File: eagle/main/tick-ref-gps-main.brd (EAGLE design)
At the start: 91.4 x 106.3 mm, 53 parts, among them CN1 1PPS Out, CN2 ISP, CN3 RS232, CN4 Power In, CN5 Serial Program, U1 ATMEGA168-AU, U2 AS1115, U3 MAX232, U4 LM2931_FIXED, X1 16MHz

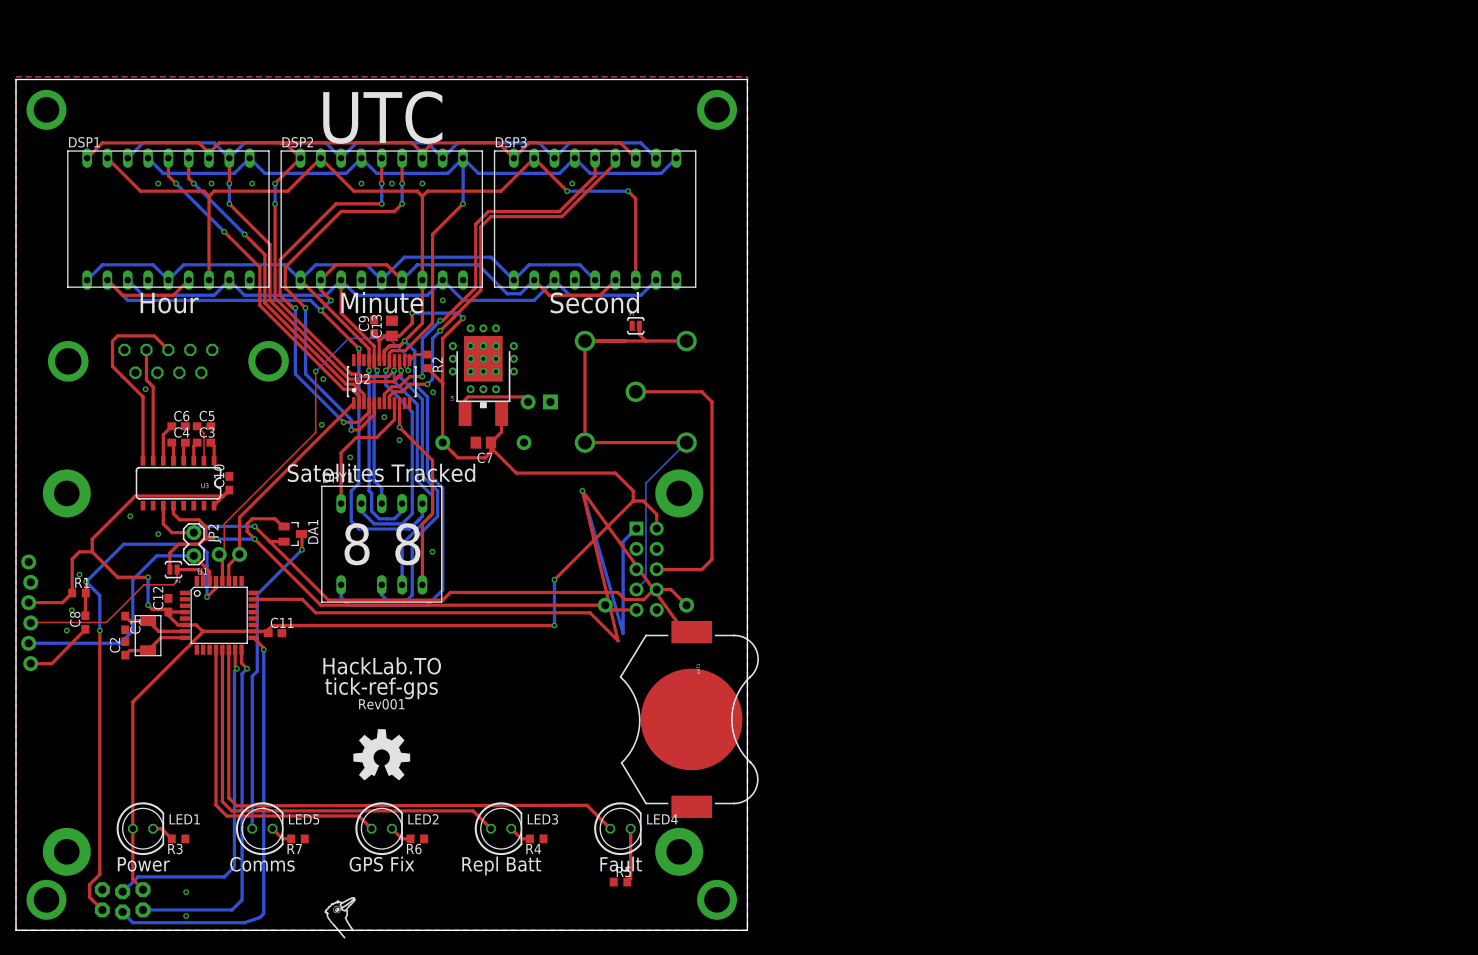
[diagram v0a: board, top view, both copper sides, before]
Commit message: New main board design schematic done, half-routed.
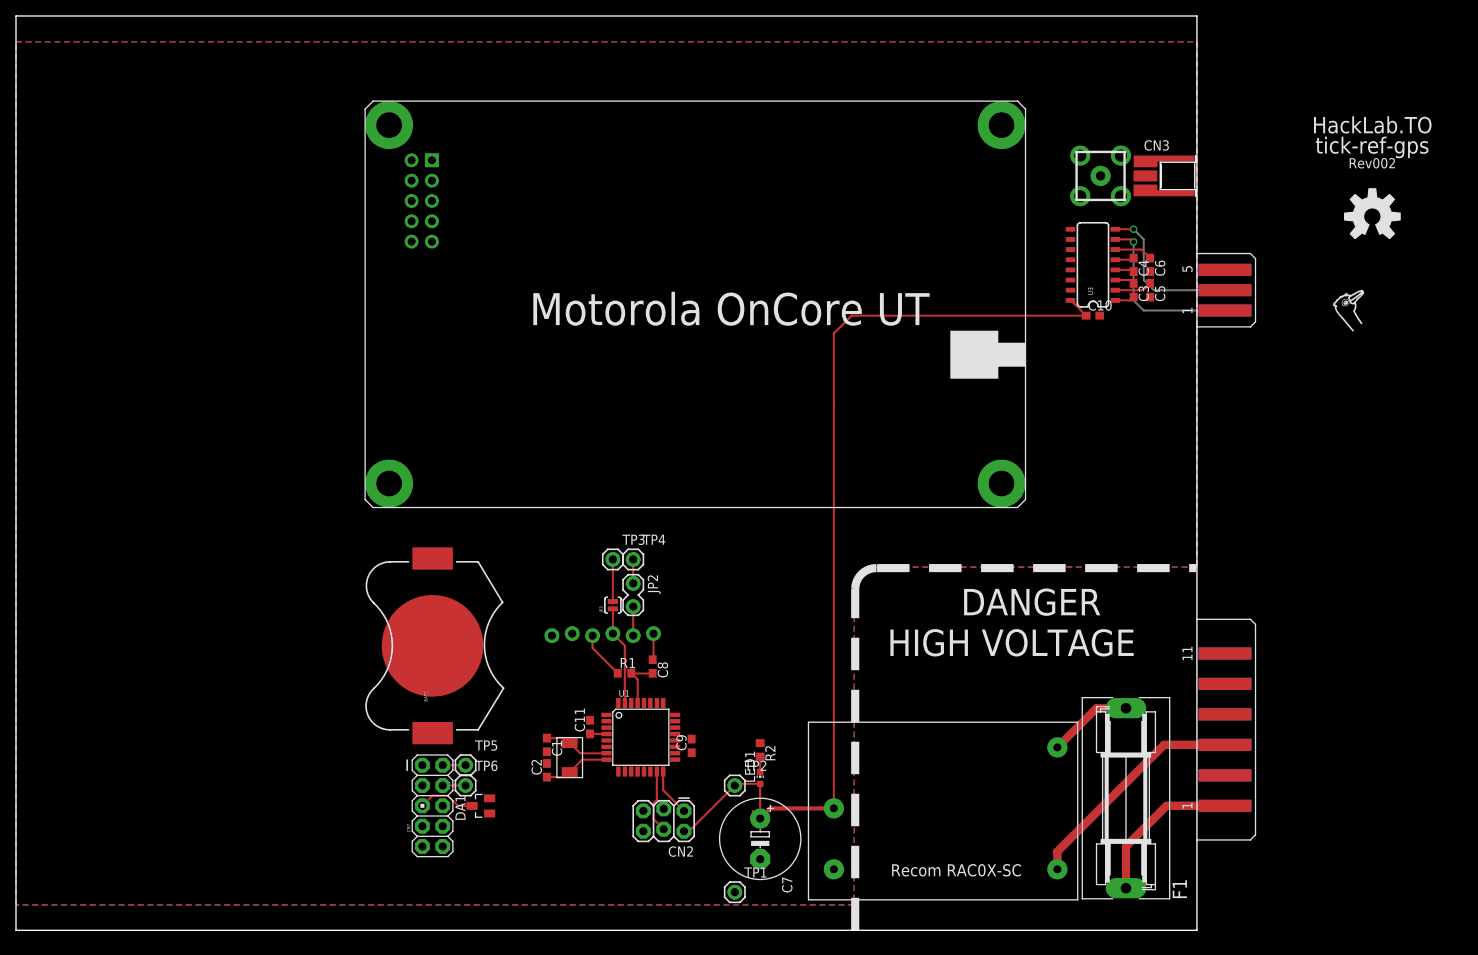
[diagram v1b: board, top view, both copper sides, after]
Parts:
- removed C12: 0.1uF, rcl:C0603
- removed C13: 2.2uF, rcl:C0805
- removed DPY1: Sats Tracked, led-sen:LDD-F302NI
- removed DSP1: Hour, display-hp:HDSP-R
- removed DSP2: Minute, display-hp:HDSP-R
- removed DSP3: Second, display-hp:HDSP-R
- removed JP1: PPS RTN Link, SparkFun:SJ_2S-NO
- removed LED2: GPS Fix, led:LED5MM
- removed LED3: Replace Batt, led:LED5MM
- removed LED4: Fault, led:LED5MM
- removed LED5: Comms, led:LED5MM
- removed R3, R4, R5: 1.8k, rcl:R0603
- removed R6: 100, rcl:R0603
- removed R7: 18, rcl:R0603
- removed U4: LM2931_FIXED, SparkFun-PowerIC:DPAK
- added CN6: Backplane, con-sen:EDGECON-M-0.1-6
- added CN7: Front Panel, SparkFun-Connectors:AVR_ICSP
- added F1: 1A Slow Blow, fuse:SH22,5A
- C7: value 2.2uF -> 330uF; device rcl:C0805 -> rcl:E5-10,5
- CN1: value 1PPS Out -> Power In; device con-coax:B35N57 -> con-sen:EDGECON-M-0.15-12
- CN3: value RS232 -> Ant. BP; device con-subd:F09VP -> con-samtec:MMCX-J-P-X-ST-EM1-MKT
- CN4: value Power In -> Ant. GPS; device SparkFun:MOLEX-1X2_LOCK -> con-sen:MOLEX-MCX-V
- JP3: value Standalone/PC -> PC Listen
- LED1: device led:LED5MM -> led:CHIP-LED0603
- R2: value 15k -> 1.8k
- U2: value AS1115 -> RAC02-05SC; device austria-sen:QSOP24 -> recom-sen:RAC0X-SC
- moved U$2 147.1 mm to (166.4, 76.9)
- moved U$1 141.1 mm to (169.5, 89.2)
- moved CN3 130.3 mm to (147.3, 94.3), flipped to the top, turned to 270 degrees
- moved GPS1 125.6 mm to (123.2, 100.6), flipped to the top
- moved C6 123.1 mm to (141.7, 83.2), turned to 270 degrees
- moved C4 121.4 mm to (139.7, 83.2), turned to 270 degrees
- moved C5 119.5 mm to (141.7, 80.0), turned to 270 degrees
- moved C3 117.8 mm to (139.7, 80.0), turned to 270 degrees
- moved U3 117.5 mm to (134.6, 83.2), turned to 90 degrees
- moved C10 110.0 mm to (134.6, 76.8), turned to 0 degrees
- moved U2 88.2 mm to (114.9, 14.0), turned to 180 degrees
- moved CN1 84.9 mm to (151.1, 25.1), flipped to the top, turned to 90 degrees
- moved LED1 77.4 mm to (93.0, 19.1)
- moved CN4 74.5 mm to (135.6, 94.3), flipped to the top
- moved C8 71.1 mm to (79.6, 33.0), turned to 270 degrees
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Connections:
- removed net CATH_HOUR_LS: DSP1.13, U2.3
- removed net CATH_HOUR_MS: DSP1.14, U2.2
- removed net CATH_MIN_LS: DSP2.13, U2.5
- removed net CATH_MIN_MS: DSP2.14, U2.4
- removed net CATH_SATS_LS: DPY1.5, U2.10
- removed net CATH_SATS_MS: DPY1.10, U2.9
- removed net CATH_SEC_LS: DSP3.13, U2.8
- removed net CATH_SEC_MS: DSP3.14, U2.7
- removed net LED1_R: LED1.K, R3.2
- removed net LED2_R: LED2.K, R6.2
- removed net LED3_R: LED3.K, R4.2
- removed net LED4_R: LED4.K, R5.2
- removed net LED5_D: DA1.3, LED5.A
- removed net LED5_R: LED5.K, R7.2
- removed net LED_ISET: R2.1, U2.13
- removed net LED_SEG_A: DPY1.3, DSP1.11, DSP1.16, DSP2.11, DSP2.16, DSP3.11, DSP3.16, U2.15
- removed net LED_SEG_B: DPY1.9, DSP1.10, DSP1.15, DSP2.10, DSP2.15, DSP3.10, DSP3.15, U2.17
- removed net LED_SEG_C: DPY1.8, DSP1.3, DSP1.8, DSP2.3, DSP2.8, DSP3.3, DSP3.8, U2.20
- removed net LED_SEG_D: DPY1.6, DSP1.2, DSP1.6, DSP2.2, DSP2.6, DSP3.2, DSP3.6, U2.23
- removed net LED_SEG_E: DPY1.7, DSP1.1, DSP1.5, DSP2.1, DSP2.5, DSP3.1, DSP3.5, U2.21
- removed net LED_SEG_F: DPY1.4, DSP1.12, DSP1.18, DSP2.12, DSP2.18, DSP3.12, DSP3.18, U2.16
- removed net LED_SEG_G: DPY1.1, DSP1.17, DSP1.7, DSP2.17, DSP2.7, DSP3.17, DSP3.7, U2.18
- removed net VIN: CN4.2, U4.1
- new net ANTENNA-GND: CN3.2@1, CN4.GND1, CN4.GND2, CN4.GND3, CN4.GND4
- new net ANTENNA-RF: CN3.1, CN4.CTR
- new net LED_COMM: CN7.5, DA1.3
- new net LINE: F1.2, U2.2
- new net LINE-PREFUSE: CN1.1, CN1.2, F1.1
- new net N$1: LED1.C, R2.2
- new net NEUTRAL: CN1.5, CN1.6, U2.1
- new net PE: CN1.11, CN1.12
- net +5V: now also C7.+, CN7.9, U2.4; no longer C12.1, C13.1, C7.1, R2.2, U2.19, U4.3
- net 1PPS: now also CN6.2; no longer CN1.1
- net 1PPS_RTN: now also CN6.6; no longer CN1.2, CN1.3, CN1.4, CN1.5, JP1.2
- net GND: now also C7.-, CN3.2@2, CN3.2@3, CN3.2@4, CN6.5, CN7.10, R2.1, U2.3; no longer C12.2, C13.2, C7.2, CN3.5, CN4.1, GPS1.MOUNT1, GPS1.MOUNT2, GPS1.MOUNT3, GPS1.MOUNT4, JP1.1, R3.1, R4.1, R5.1, R6.1, R7.1, U2.6, U4.4
- net GPS_RX: now also DA1.2; no longer DA1.1
- net GPS_RX_HV: now also CN6.3; no longer CN3.3
- net GPS_TX: now also DA1.1; no longer DA1.2
- net GPS_TX_HV: now also CN6.1; no longer CN3.2
- net LED_BATT: now also CN7.3; no longer LED3.A
- net LED_FAULT: now also CN7.1; no longer LED4.A
- net LED_GPSFIX: now also CN7.7; no longer LED2.A
- net SCL: now also CN7.2; no longer U2.14
- net SDA: now also CN7.4; no longer U2.1
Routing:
- net LED_SEG_G: track 172.6 -> 0.00 mm, vias 3 -> 0
- net LED_SEG_A: track 154.8 -> 0.00 mm, vias 3 -> 0
- net LED_SEG_F: track 148.8 -> 0.00 mm, vias 3 -> 0
- net LED_SEG_B: track 133.3 -> 0.00 mm, vias 2 -> 0
- net LED_SEG_D: track 131.4 -> 0.00 mm, vias 3 -> 0
- net VBATT: track 123.4 -> 0.00 mm, vias 1 -> 0
- net LED_SEG_E: track 110.3 -> 0.00 mm, vias 1 -> 0
- net +5V: track 235.7 -> 130.0 mm, vias 6 -> 0
- net LED_SEG_C: track 104.8 -> 0.00 mm, vias 1 -> 0
- net GPS_RX: track 80.2 -> 5.26 mm, vias 2 -> 0
- net GPS_TX: track 76.3 -> 3.00 mm, vias 1 -> 0
- net LED_FAULT: track 67.8 -> 0.00 mm
- net AVR_RESET: track 72.7 -> 6.72 mm, vias 3 -> 0
- net 1PPS_RTN: track 65.8 -> 0.00 mm
- net NEUTRAL: track 0.00 -> 57.4 mm
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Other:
- board size 91.4 x 106.3 mm -> 147.6 x 114.3 mm
- board text added: "DANGER"
- board text added: "HIGH VOLTAGE"
- board text added: "Rev002"
- board text removed: "+"
- board text removed: "-"
- board text removed: "1PPS Out"
- board text removed: "6-20VDC"
- board text removed: "Comms"
- board text removed: "Fault"
- board text removed: "GPS Fix"
- board text removed: "Hour"
- board text removed: "ISP"
- board text removed: "Minute"
- board text removed: "Power"
- board text removed: "RS232"
- board text removed: "Repl Batt"
- board text removed: "Rev001"
- board text removed: "Satellites Tracked"
- board text removed: "Second"
- board text removed: "Serial Program"
- board text removed: "UTC"

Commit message: Finished routing board, need to run through checklist tomorrow before CAMing.
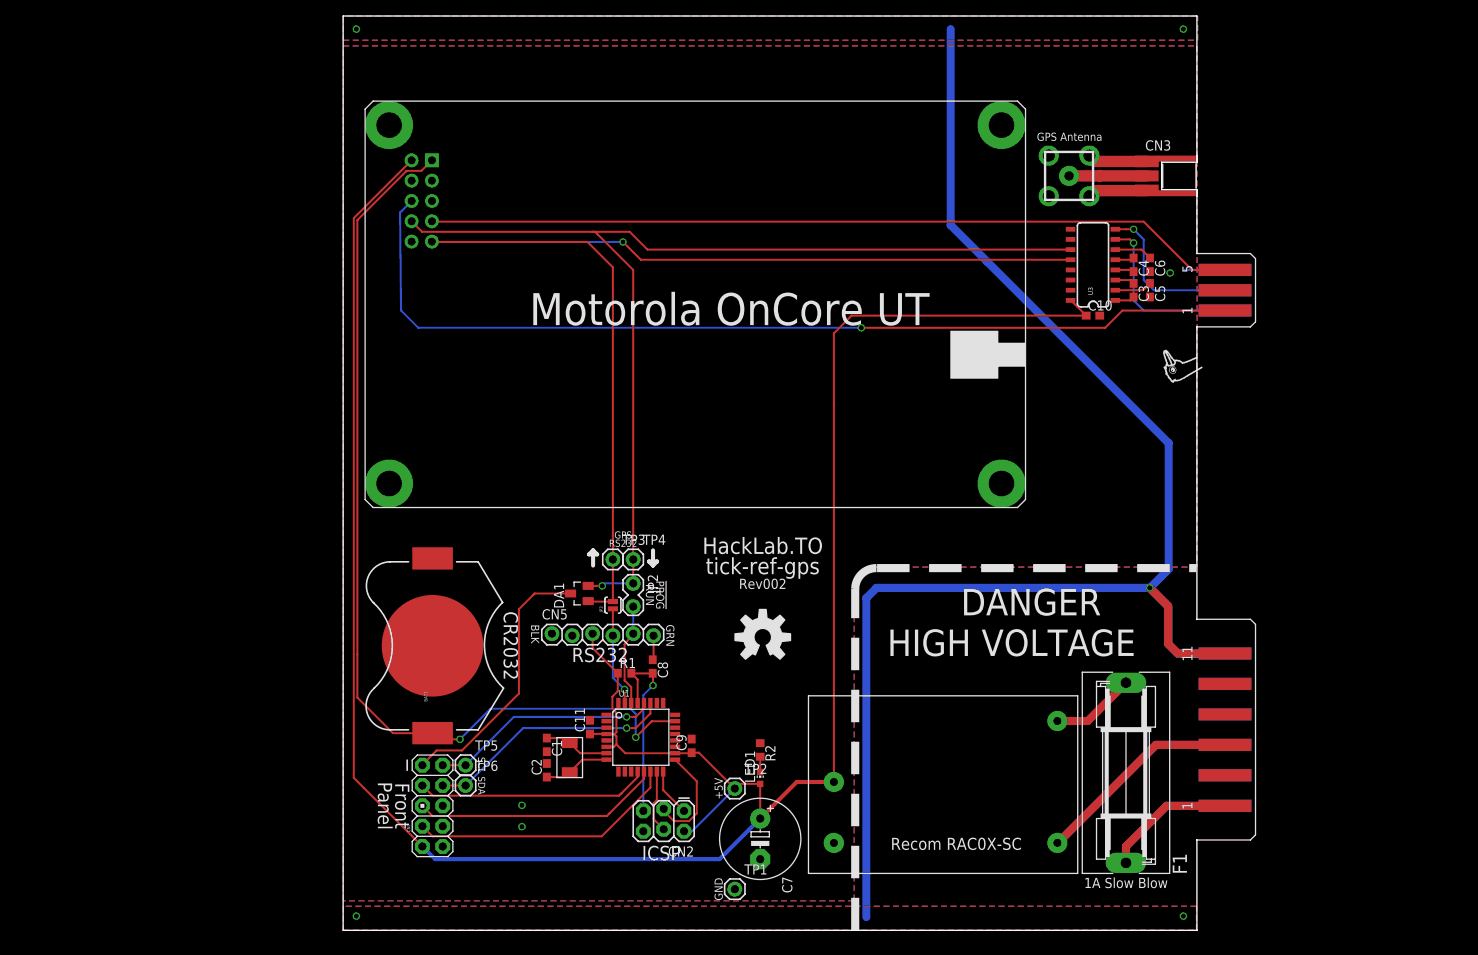
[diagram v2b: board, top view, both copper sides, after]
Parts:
- moved U$1 92.6 mm to (93.3, 36.6)
- moved DA1 29.3 mm to (70.4, 42.1)
- moved U$2 21.4 mm to (146.2, 69.9), turned to 120 degrees
- moved CN4 3.94 mm to (131.6, 94.3)
- moved U2 3.30 mm to (114.9, 17.3)
- moved F1 3.17 mm to (138.7, 19.7)
- moved TP1 0.38 mm to (89.9, 5.14)
- moved TP2 0.38 mm to (89.9, 17.7)
- moved CN5 0.25 mm to (67.0, 37.1), flipped to the top, turned to 0 degrees
- moved CN3 0.17 mm to (147.5, 94.3)
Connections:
- net N$1 renamed LED1_R
- net GPS_RX: now also DA1.1; no longer DA1.2
- net GPS_TX: now also DA1.2; no longer DA1.1
- net LED_BATT: now also CN7.5; no longer CN7.3
- net LED_COMM: now also CN7.1; no longer CN7.5
- net LED_FAULT: now also CN7.7; no longer CN7.1
- net LED_GPSFIX: now also CN7.3; no longer CN7.7
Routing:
- net PE: track 0.00 -> 206.1 mm, vias 0 -> 5
- net +5V: track 130.0 -> 293.4 mm
- net GPS_RX: track 5.26 -> 149.6 mm, vias 0 -> 1
- net GPS_TX: track 3.00 -> 135.8 mm, vias 0 -> 1
- net VBATT: track 0.00 -> 119.6 mm, vias 0 -> 2
- net 1PPS: track 0.00 -> 119.1 mm, vias 0 -> 1
- net 1PPS_RTN: track 0.00 -> 101.7 mm
- net LED_FAULT: track 0.00 -> 33.6 mm
- net LED_BATT: track 0.00 -> 31.1 mm
- net LED_GPSFIX: track 0.00 -> 29.1 mm
- net SDA: track 2.86 -> 31.0 mm, vias 0 -> 1
- net LED_COMM: track 7.25 -> 33.8 mm
- net SCL: track 2.86 -> 28.8 mm, vias 0 -> 1
- net AVR_RESET: track 6.72 -> 24.4 mm, vias 0 -> 1
- net ANTENNA-GND: track 0.00 -> 15.0 mm
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- added copper zone on layer 1, net PE
- added copper zone on layer 16, net PE
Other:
- board size 147.6 x 114.3 mm -> 106.7 x 114.3 mm
- board text added: "!PROG"
- board text added: "+5V"
- board text added: "1A Slow Blow"
- board text added: "BLK"
- board text added: "CR2032"
- board text added: "Front"
- board text added: "GND"
- board text added: "GPS"
- board text added: "GPS Antenna"
- board text added: "GRN"
- board text added: "ICSP"
- board text added: "Panel"
- board text added: "RS232"
- board text added: "RUN"
- board text added: "SCL"
- board text added: "SDA"

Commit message: Board checklist complete except for printing it out and comparing it to the existing modules connector-alignment-wise and size-wise.
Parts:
- moved C1 40.9 mm to (25.5, 23.2)
- moved C10 40.9 mm to (93.7, 76.8)
- moved C2 40.9 mm to (25.5, 20.0)
- moved C7 40.9 mm to (52.1, 11.4)
- moved C8 40.9 mm to (38.7, 33.0)
- moved CN4 40.9 mm to (90.7, 94.3)
- moved CN5 40.9 mm to (26.1, 37.1)
- moved F1 40.9 mm to (97.9, 19.7)
- moved JP2 40.9 mm to (36.3, 43.2)
- moved LED1 40.9 mm to (52.1, 19.1)
- moved R2 40.9 mm to (52.1, 22.5)
- moved TP1 40.9 mm to (49.0, 5.14)
- moved TP2 40.9 mm to (49.0, 17.7)
- moved TP4 40.9 mm to (36.3, 46.4)
- moved U1 40.9 mm to (37.2, 24.1)
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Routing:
- added copper zone on layer 1, net ANTENNA-RF
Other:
- board text added: "http://hackstrich.sen.cx/HackLab.TO_Timing_Reference_A"
